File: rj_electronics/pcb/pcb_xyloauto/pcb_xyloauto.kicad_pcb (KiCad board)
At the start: 2 copper layers, 200 x 37 mm, 21 parts, among them J1 Screw_Terminal_01x08, J3 Conn_01x02_Pin, J4 Barrel_Jack, J5 Screw_Terminal_01x08, U1 Sparkfun_Pro_Micro, U2 ULN2803A, U3 LM317_TO-220

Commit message: nc
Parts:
- moved RV1 4.47 mm to (53.7, 138.0)
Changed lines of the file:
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@@
   )
   (footprint "Potentiometer_THT:Potentiometer_Bourns_3299W_Vertical" (layer "F.Cu")
-    (at 55.5493 133.9441 180)
+    (at 53.68348 138.003745 180)
     (descr "Potentiometer, vertical, Bourns 3299W, https://www.bourns.com/pdfs/3299.pdf")
     (tags "Potentiometer vertical Bourns 3299W")
@@
     (property "ki_keywords" "resistor variable trimpot trimmer")
     (attr through_hole)
-    (fp_text reference "RV1" (at -2.54 -3.16 180) (layer "F.SilkS")
+    (fp_text reference "RV1" (at -3.49139 2.777399 180) (layer "F.SilkS")
         (effects (font (size 1 1) (thickness 0.15)))
     )

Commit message: nc
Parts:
- moved D4 3.38 mm to (108.0, 139.3)
- moved D5 2.32 mm to (151.0, 139.3)
- moved R5 2.29 mm to (190.1, 141.5)
- moved D6 2.21 mm to (193.9, 139.3)
- moved R3 2.13 mm to (114.2, 141.5)
- moved R4 1.29 mm to (147.3, 141.5)
- moved R2 1.26 mm to (71.6, 141.5)
- moved D3 0.97 mm to (65.0, 139.3)
- moved J3 0.32 mm to (67.6, 133.8)
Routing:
- net VOUT: track 0.00 -> 226.8 mm
- net GND: track 0.00 -> 215.5 mm
- net Net-(D2-A): track 0.00 -> 174.5 mm
- net LED4: track 0.00 -> 158.1 mm, vias 0 -> 1
- net VIN: track 0.00 -> 132.0 mm
- net LED3: track 0.00 -> 116.8 mm
- net LED2: track 0.00 -> 66.4 mm, vias 0 -> 1
- net Net-(J1-Pin_8): track 0.00 -> 41.7 mm
- net Net-(U1-D2): track 0.00 -> 41.0 mm
- net Net-(U1-~D3): track 0.00 -> 37.4 mm
- net Net-(J1-Pin_7): track 0.00 -> 37.1 mm
- net Net-(U1-D4/A6): track 0.00 -> 33.8 mm
- net Net-(J1-Pin_6): track 0.00 -> 32.6 mm
- net Net-(U1-~D5): track 0.00 -> 30.2 mm
- net LED1: track 0.00 -> 28.3 mm, vias 0 -> 1
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
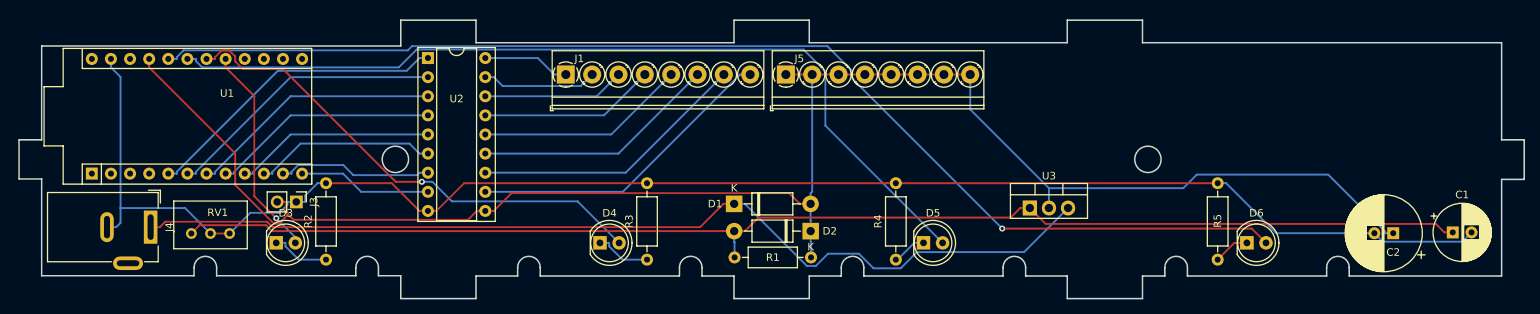
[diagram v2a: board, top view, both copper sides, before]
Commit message: LED holes
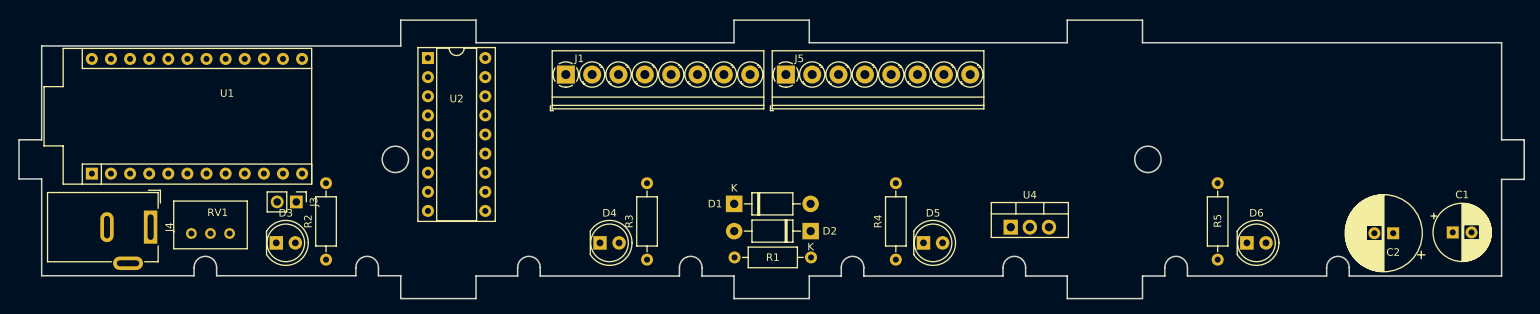
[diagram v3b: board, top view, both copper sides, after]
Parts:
- removed U3: LM317_TO-220, Package_TO_SOT_THT:TO-220-3_Vertical
- added U4: LM317_TO-220, Package_TO_SOT_THT:TO-220-3_Vertical, F.Cu at (162.6, 137.2)
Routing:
- net VOUT: track 226.8 -> 0.00 mm
- net GND: track 215.5 -> 0.00 mm
- net Net-(D2-A): track 174.5 -> 0.00 mm
- net LED4: track 158.1 -> 0.00 mm, vias 1 -> 0
- net VIN: track 132.0 -> 0.00 mm
- net LED3: track 116.8 -> 0.00 mm
- net LED2: track 66.4 -> 0.00 mm, vias 1 -> 0
- net Net-(J1-Pin_8): track 41.7 -> 0.00 mm
- net Net-(U1-D2): track 41.0 -> 0.00 mm
- net Net-(U1-~D3): track 37.4 -> 0.00 mm
- net Net-(J1-Pin_7): track 37.1 -> 0.00 mm
- net Net-(U1-D4/A6): track 33.8 -> 0.00 mm
- net Net-(J1-Pin_6): track 32.6 -> 0.00 mm
- net Net-(U1-~D5): track 30.2 -> 0.00 mm
- net LED1: track 28.3 -> 0.00 mm, vias 1 -> 0
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
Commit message: nc
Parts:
- moved J3 9.19 mm to (74.5, 127.8)
- moved D6 2.65 mm to (193.4, 136.7)
- moved D5 2.64 mm to (150.5, 136.7)
- moved D3 2.64 mm to (64.5, 136.7)
- moved D4 2.51 mm to (107.6, 136.8)
- moved R2 2.10 mm to (73.7, 141.7)
- moved R4 0.99 mm to (146.3, 141.5)
- moved R5 0.34 mm to (189.7, 141.6)
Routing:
- net VOUT: track 0.00 -> 223.2 mm
- net GND: track 0.00 -> 220.4 mm
- net Net-(D2-A): track 0.00 -> 175.4 mm
- net LED4: track 0.00 -> 155.5 mm
- net VIN: track 0.00 -> 122.4 mm
- net LED3: track 0.00 -> 113.1 mm
- net LED2: track 0.00 -> 63.7 mm, vias 0 -> 1
- net LED1: track 0.00 -> 42.8 mm
- net Net-(J1-Pin_8): track 0.00 -> 41.7 mm
- net Net-(U1-D2): track 0.00 -> 41.0 mm
- net Net-(U1-~D3): track 0.00 -> 37.4 mm
- net Net-(J1-Pin_7): track 0.00 -> 37.1 mm
- net Net-(U1-D4/A6): track 0.00 -> 33.8 mm
- net Net-(J1-Pin_6): track 0.00 -> 32.6 mm
- net Net-(U1-~D5): track 0.00 -> 30.2 mm
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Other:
- outline, holes or cut-outs redrawn

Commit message: nc
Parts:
- moved U4 2.48 mm to (165.0, 137.7)
- moved C1 0.84 mm to (221.1, 137.0)
- moved C2 0.70 mm to (213.2, 137.3)
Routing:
- net VIN: track 122.4 -> 125.0 mm
- net VOUT: track 223.2 -> 222.2 mm
